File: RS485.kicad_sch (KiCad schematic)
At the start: 5 parts, among them J11 Screw_Terminal_01x05, SW3 SW_DIP_x03, U3 SIT3490EESA

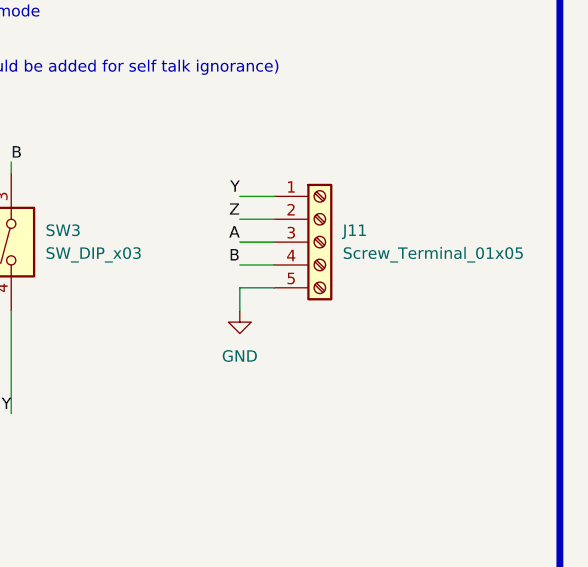
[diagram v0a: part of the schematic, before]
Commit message: Key CHanges for connector choices , termination and semi-final decisions on them
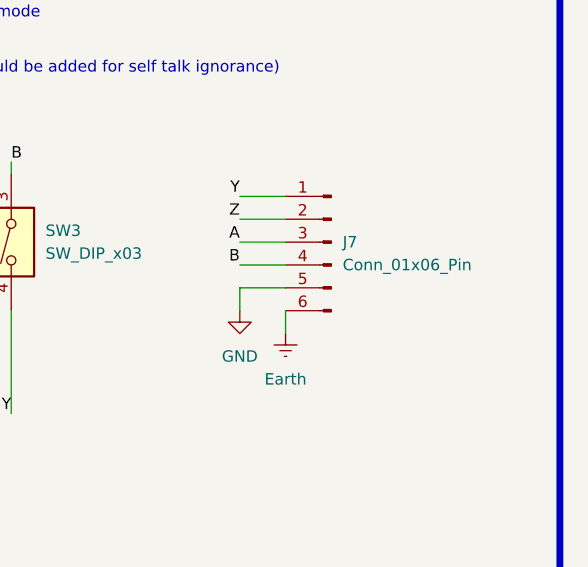
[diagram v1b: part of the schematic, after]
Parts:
- removed J11: Screw_Terminal_01x05, TerminalBlock_Phoenix:TerminalBlock_Phoenix_PT-1,5-5-3.5-H_1x05_P3.50mm_Horizontal, symbol Connector:Screw_Terminal_01x05
- added J7: Conn_01x06_Pin, Connector_JST:JST_XH_B6B-XH-A_1x06_P2.50mm_Vertical, symbol Connector:Conn_01x06_Pin
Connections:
- net A: now also J7.3 (Pin_3)
- net B: now also J7.4 (Pin_4)
- net GND: now also J7.5 (Pin_5)
- net Y: now also J7.1 (Pin_1)
- net Z: now also J7.2 (Pin_2)
- new net Earth: J7.6 (Pin_6)
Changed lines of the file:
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@@
+	(wire
+		(pts
+			(xy 172.72 104.14) (xy 172.72 106.68)
+		)
+		(stroke
+			(width 0)
+			(type default)
+		)
+	)
 	(wire
 		(pts
@@
 	(wire
 		(pts
-			(xy 167.64 91.44) (xy 171.45 91.44)
+			(xy 167.64 91.44) (xy 172.72 91.44)
 		)
 		(stroke
@@
 	(wire
 		(pts
-			(xy 167.64 99.06) (xy 171.45 99.06)
-		)
-		(stroke
-			(width 0)
-			(type default)
-		)
-	)
-	(wire
-		(pts
-			(xy 167.64 101.6) (xy 171.45 101.6)
-		)
-		(stroke
-			(width 0)
-			(type default)
-		)
-	)
-	(wire
-		(pts
-			(xy 167.64 96.52) (xy 171.45 96.52)
+			(xy 167.64 99.06) (xy 172.72 99.06)
+		)
+		(stroke
+			(width 0)
+			(type default)
+		)
+	)
+	(wire
+		(pts
+			(xy 167.64 101.6) (xy 172.72 101.6)
+		)
+		(stroke
+			(width 0)
+			(type default)
+		)
+	)
+	(wire
+		(pts
+			(xy 167.64 96.52) (xy 172.72 96.52)
 		)
 		(stroke
@@
 	(wire
 		(pts
-			(xy 167.64 93.98) (xy 171.45 93.98)
+			(xy 167.64 93.98) (xy 172.72 93.98)
 		)
 		(stroke
@@
 				(path "/38f33acd-ac87-4918-9c1f-d78977d10c9f/eaedeb33-b3bd-4866-a006-654b07613880"
 					(reference "#PWR038")
+					(unit 1)
+				)
+			)
+		)
+	)
+	(symbol
+		(lib_id "power:Earth")
+		(at 172.72 106.68 0)
+		(unit 1)
+		(exclude_from_sim no)
+		(in_bom yes)
+		(on_board yes)
+		(dnp no)
+		(fields_autoplaced yes)
+		(property "Reference" "#PWR030"
+			(at 172.72 113.03 0)
+			(effects
+				(font
+					(size 1.27 1.27)
+				)
+				(hide yes)
+			)
+		)
+		(property "Value" "Earth"
+			(at 172.72 111.76 0)
+			(effects
+				(font
+					(size 1.27 1.27)
+				)
+			)
+		)
+		(property "Footprint" ""
+			(at 172.72 106.68 0)
+			(effects
+				(font
+					(size 1.27 1.27)
+				)
+				(hide yes)
+			)
+		)
+		(property "Datasheet" "~"
+			(at 172.72 106.68 0)
+			(effects
+				(font
+					(size 1.27 1.27)
+				)
+				(hide yes)
+			)
+		)
+		(property "Description" "Power symbol creates a global label with name \"Earth\""
+			(at 172.72 106.68 0)
+			(effects
+				(font
+					(size 1.27 1.27)
+				)
+				(hide yes)
+			)
+		)
+		(pin "1"
+		)
+		(instances
+			(project "OhWare"
+				(path "/38f33acd-ac87-4918-9c1f-d78977d10c9f/eaedeb33-b3bd-4866-a006-654b07613880"
+					(reference "#PWR030")
 					(unit 1)
 				)
@@
 	)
 	(symbol
+		(lib_id "Connector:Conn_01x06_Pin")
+		(at 177.8 96.52 0)
+		(mirror y)
+		(unit 1)
+		(exclude_from_sim no)
+		(in_bom yes)
+		(on_board yes)
+		(dnp no)
+		(fields_autoplaced yes)
+		(property "Reference" "J7"
+			(at 179.07 96.5199 0)
+			(effects
+				(font
+					(size 1.27 1.27)
+				)
+				(justify right)
+			)
+		)
+		(property "Value" "Conn_01x06_Pin"
+			(at 179.07 99.0599 0)
+			(effects
+				(font
+					(size 1.27 1.27)
+				)
+				(justify right)
+			)
+		)
+		(property "Footprint" "Connector_JST:JST_XH_B6B-XH-A_1x06_P2.50mm_Vertical"
+			(at 177.8 96.52 0)
+			(effects
+				(font
+					(size 1.27 1.27)
+				)
+				(hide yes)
+			)
+		)
+		(property "Datasheet" "~"
+			(at 177.8 96.52 0)
+			(effects
+				(font
+					(size 1.27 1.27)
+				)
+				(hide yes)
+			)
+		)
+		(property "Description" "Generic connector, single row, 01x06, script generated"
+			(at 177.8 96.52 0)
+			(effects
+				(font
+					(size 1.27 1.27)
+				)
+				(hide yes)
+			)
+		)
+		(pin "5"
+		)
+		(pin "2"
+		)
+		(pin "4"
+		)
+		(pin "1"
+		)
+		(pin "3"
+		)
+		(pin "6"
+		)
+		(instances
+			(project ""
+				(path "/38f33acd-ac87-4918-9c1f-d78977d10c9f/eaedeb33-b3bd-4866-a006-654b07613880"
+					(reference "J7")
+					(unit 1)
+				)
+			)
+		)
+	)
+	(symbol
 		(lib_id "power:GND")
 		(at 167.64 104.14 0)
@@
 					(unit 1)
 				)
-			)
-		)
-	)
-	(symbol
-		(lib_id "Connector:Screw_Terminal_01x05")
-		(at 176.53 96.52 0)
-		(unit 1)
-		(exclude_from_sim no)
-		(in_bom yes)
-		(on_board yes)
-		(dnp no)
-		(fields_autoplaced yes)
-		(property "Reference" "J11"
-			(at 179.07 95.2499 0)
-			(effects
-				(font
-					(size 1.27 1.27)
-				)
-				(justify left)
-			)
-		)
-		(property "Value" "Screw_Terminal_01x05"
-			(at 179.07 97.7899 0)
-			(effects
-				(font
-					(size 1.27 1.27)
-				)
-				(justify left)
-			)
-		)
-		(property "Footprint" "TerminalBlock_Phoenix:TerminalBlock_Phoenix_PT-1,5-5-3.5-H_1x05_P3.50mm_Horizontal"
-			(at 176.53 96.52 0)
-			(effects
-				(font
-					(size 1.27 1.27)
-				)
-				(hide yes)
-			)
-		)
-		(property "Datasheet" "~"
-			(at 176.53 96.52 0)
-			(effects
-				(font
-					(size 1.27 1.27)
-				)
-				(hide yes)
-			)
-		)
-		(property "Description" "Generic screw terminal, single row, 01x05, script generated (kicad-library-utils/schlib/autogen/connector/)"
-			(at 176.53 96.52 0)
-			(effects
-				(font
-					(size 1.27 1.27)
-				)
-				(hide yes)
-			)
-		)
-		(pin "5"
-		)
-		(pin "1"
-		)
-		(pin "4"
-		)
-		(pin "2"
-		)
-		(pin "3"
-		)
-		(instances
-			(project ""
-				(path "/38f33acd-ac87-4918-9c1f-d78977d10c9f/eaedeb33-b3bd-4866-a006-654b07613880"
-					(reference "J11")
-					(unit 1)
-				)

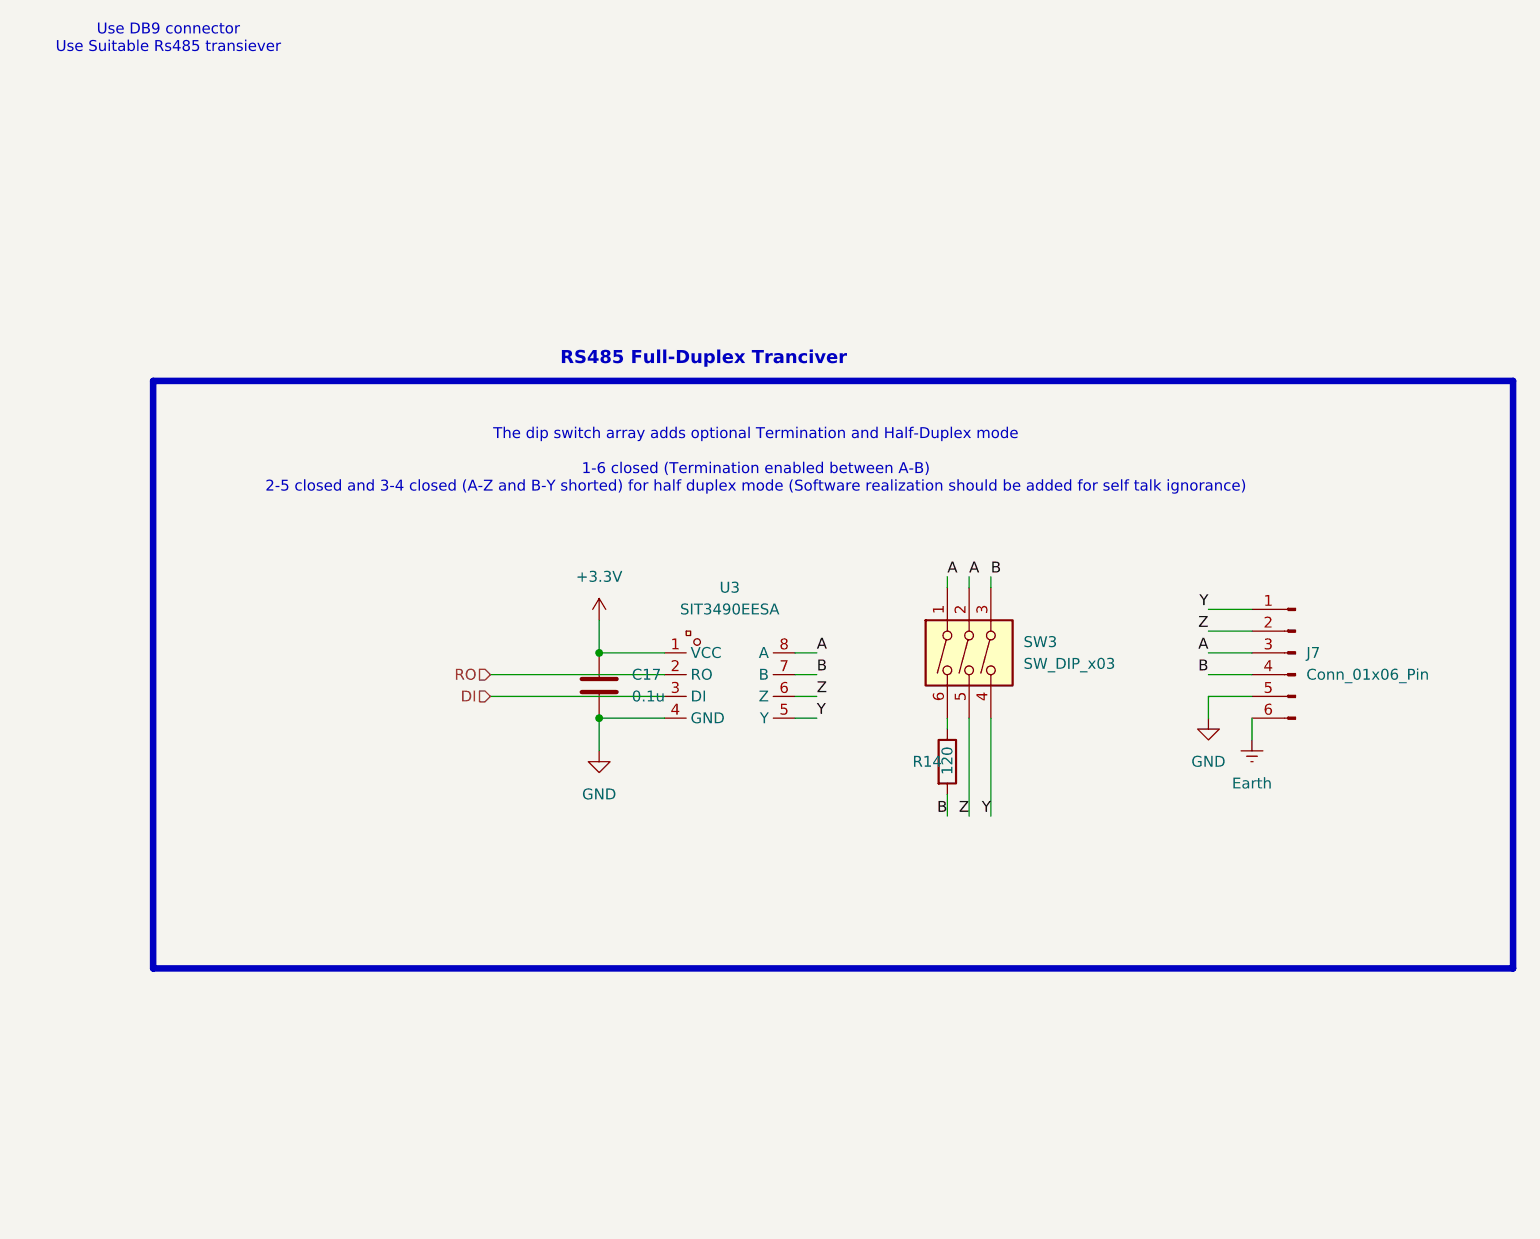
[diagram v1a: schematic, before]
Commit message: Done routing for Buck Converter , Rs485 and CAN , Some Routing for MCU and associated circuitry , NO ETHERNET ROUTING , NO module Interconnects yet
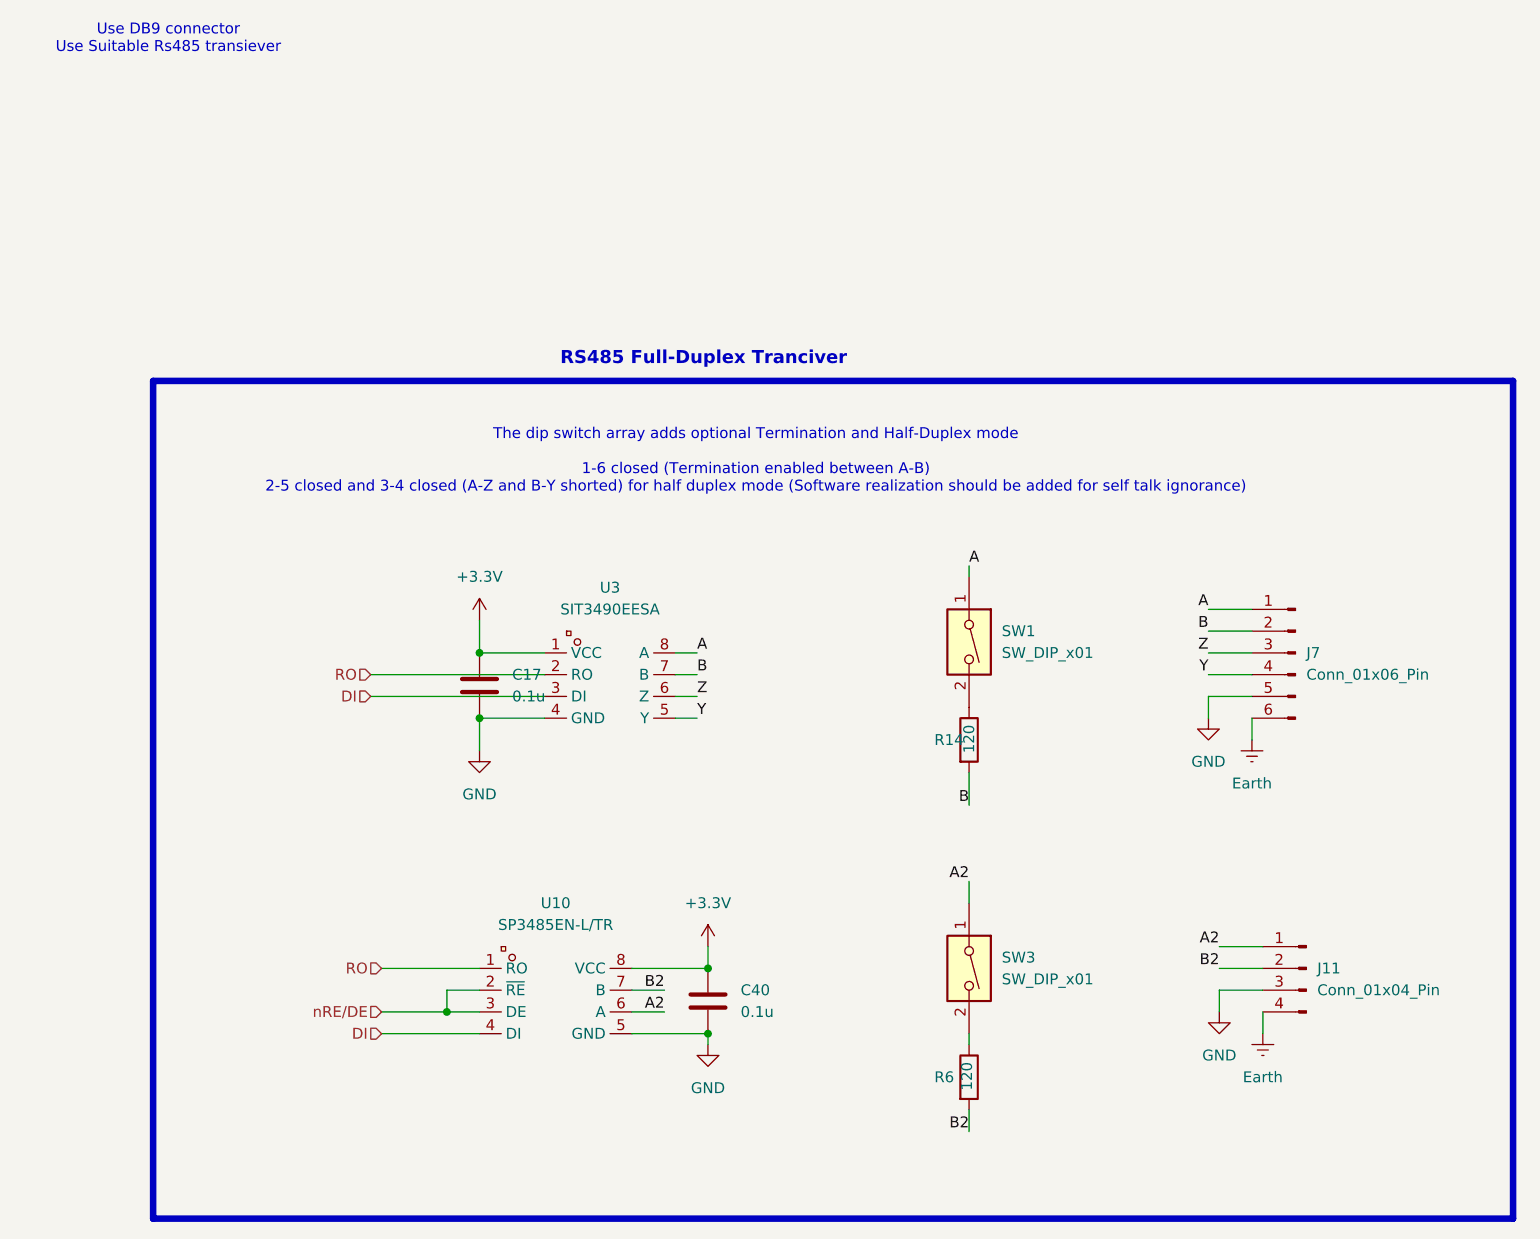
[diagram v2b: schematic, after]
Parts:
- removed SW3: SW_DIP_x03, Button_Switch_THT:SW_DIP_SPSTx03_Slide_6.7x9.18mm_W7.62mm_P2.54mm_LowProfile, symbol Switch:SW_DIP_x03
- added C40: 0.1u, Capacitor_SMD:C_0805_2012Metric, symbol Device:C
- added J11: Conn_01x04_Pin, Connector_JST:JST_XH_B4B-XH-A_1x04_P2.50mm_Vertical, symbol Connector:Conn_01x04_Pin
- added R6: 120, Resistor_SMD:R_1210_3225Metric, symbol Device:R
- added SW1, SW3: SW_DIP_x01, Button_Switch_SMD:SW_DIP_SPSTx01_Slide_6.7x4.1mm_W8.61mm_P2.54mm_LowProfile, symbol Switch:SW_DIP_x01
- added U10: SP3485EN-L/TR, EasyEDA:SOIC-8_L5.0-W4.0-P1.27-LS6.0-BL, symbol EasyEDA:SP3485EN-L_TR
- R14: footprint Resistor_SMD:R_0805_2012Metric -> Resistor_SMD:R_1210_3225Metric
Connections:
- net +3.3V: now also C40.1, U10.8 (VCC)
- net A: now also J7.1 (Pin_1), SW1.1; no longer J7.3 (Pin_3)
- net B: now also J7.2 (Pin_2); no longer J7.4 (Pin_4)
- net DI: now also U10.4 (DI)
- net Earth: now also J11.4 (Pin_4)
- net GND: now also C40.2, J11.3 (Pin_3), U10.5 (GND)
- net RO: now also U10.1 (RO)
- net Y: now also J7.4 (Pin_4); no longer J7.1 (Pin_1)
- net Z: now also J7.3 (Pin_3); no longer J7.2 (Pin_2)
- net at R14.1: now also SW1.2
- new net: R6.1, SW3.2
- new net A2: J11.1 (Pin_1), SW3.1, U10.6 (A)
- new net B2: J11.2 (Pin_2), R6.2, U10.7 (B)
- new net nRE/DE: U10.2 (~{RE}), U10.3 (DE)
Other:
- moved on the sheet: C17, R14, U3

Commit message: UPDATED
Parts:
- C17, C40: footprint Capacitor_SMD:C_0805_2012Metric -> Capacitor_SMD:C_1206_3216Metric_Pad1.33x1.80mm_HandSolder
- J11: footprint Connector_JST:JST_XH_B4B-XH-A_1x04_P2.50mm_Vertical -> Connector_JST:JST_XH_S4B-XH-A_1x04_P2.50mm_Horizontal
- J7: footprint Connector_JST:JST_XH_B6B-XH-A_1x06_P2.50mm_Vertical -> Connector_JST:JST_XH_S6B-XH-A_1x06_P2.50mm_Horizontal
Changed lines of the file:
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@@
 			)
 		)
-		(property "Footprint" "Capacitor_SMD:C_0805_2012Metric"
+		(property "Footprint" "Capacitor_SMD:C_1206_3216Metric_Pad1.33x1.80mm_HandSolder"
 			(at 110.1852 140.97 0)
 			(effects
@@
 			)
 		)
-		(property "Footprint" "Connector_JST:JST_XH_B6B-XH-A_1x06_P2.50mm_Vertical"
+		(property "Footprint" "Connector_JST:JST_XH_S6B-XH-A_1x06_P2.50mm_Horizontal"
 			(at 177.8 96.52 0)
 			(effects
@@
 			)
 		)
-		(property "Footprint" "Connector_JST:JST_XH_B4B-XH-A_1x04_P2.50mm_Vertical"
+		(property "Footprint" "Connector_JST:JST_XH_S4B-XH-A_1x04_P2.50mm_Horizontal"
 			(at 179.07 133.35 0)
 			(effects
@@
 			)
 		)
-		(property "Footprint" "Capacitor_SMD:C_0805_2012Metric"
+		(property "Footprint" "Capacitor_SMD:C_1206_3216Metric_Pad1.33x1.80mm_HandSolder"
 			(at 83.5152 104.14 0)
 			(effects
